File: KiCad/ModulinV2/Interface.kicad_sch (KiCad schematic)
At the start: 51 parts, among them IC2 TL072HIDR, IC3 ADS7041IDCUR, IC4 ADS7866IDBVT, IC42 ADS7041IDCUR, IC5 ADS7866IDBVT, IC6 DAC60501ZDGSR, IC7 DAC60501ZDGSR, IC8 TL074HIDR

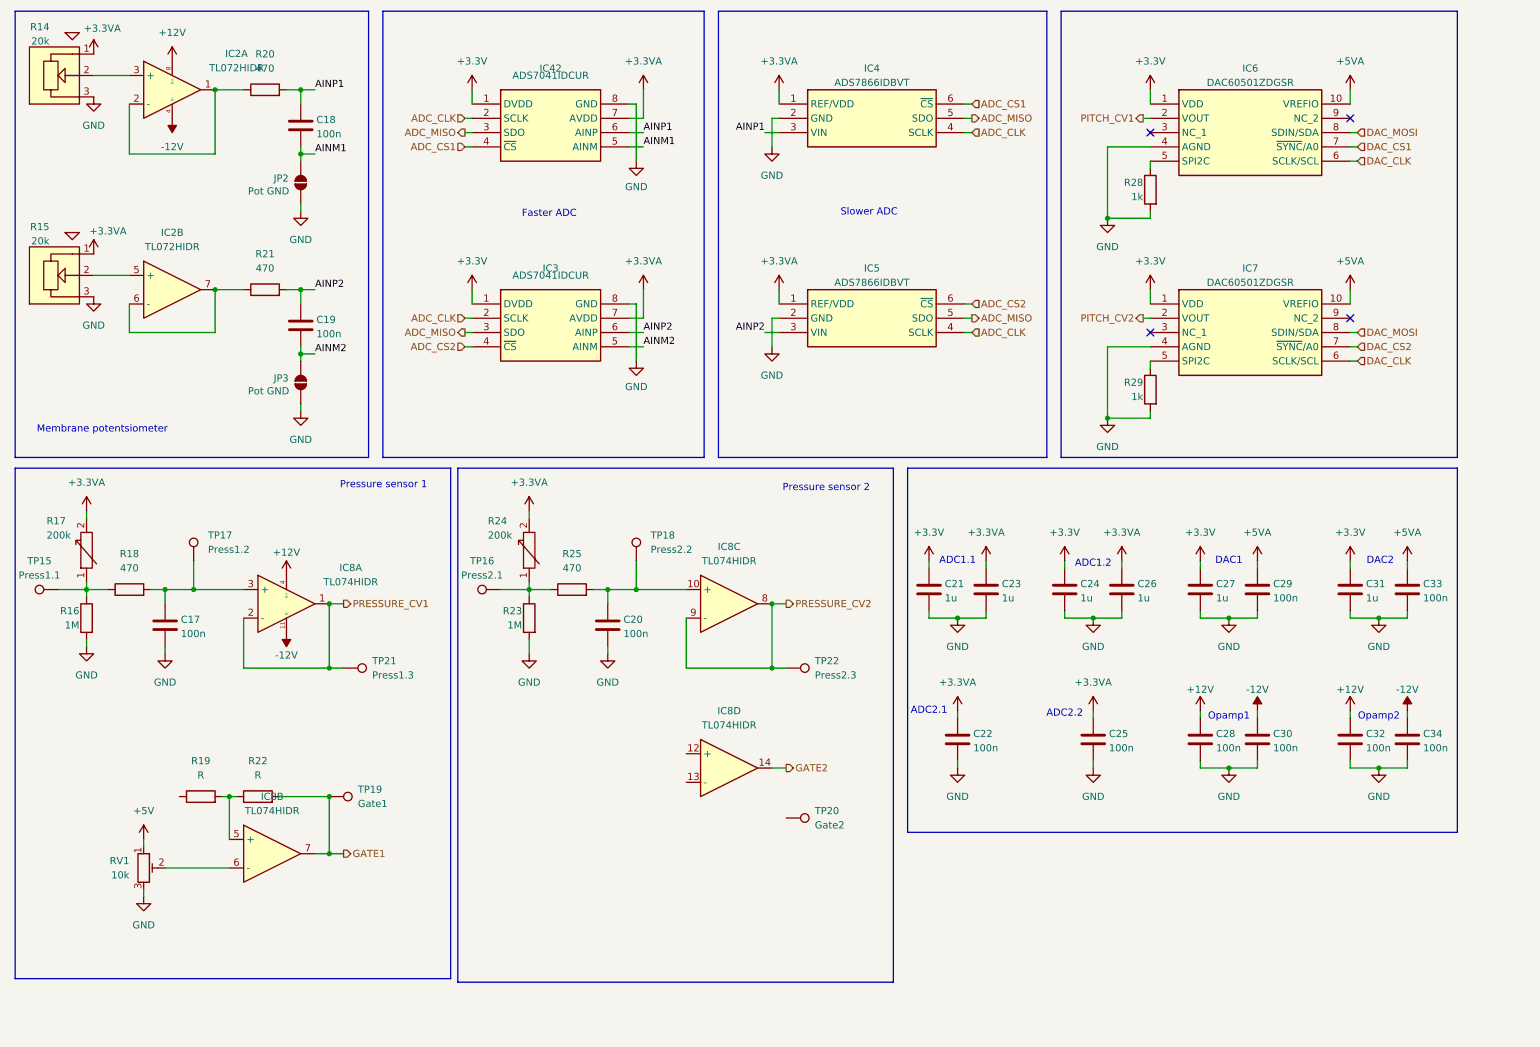
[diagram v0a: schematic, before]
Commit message: Changed switch for the boot and nrst. Fixed the GATE interface trigger
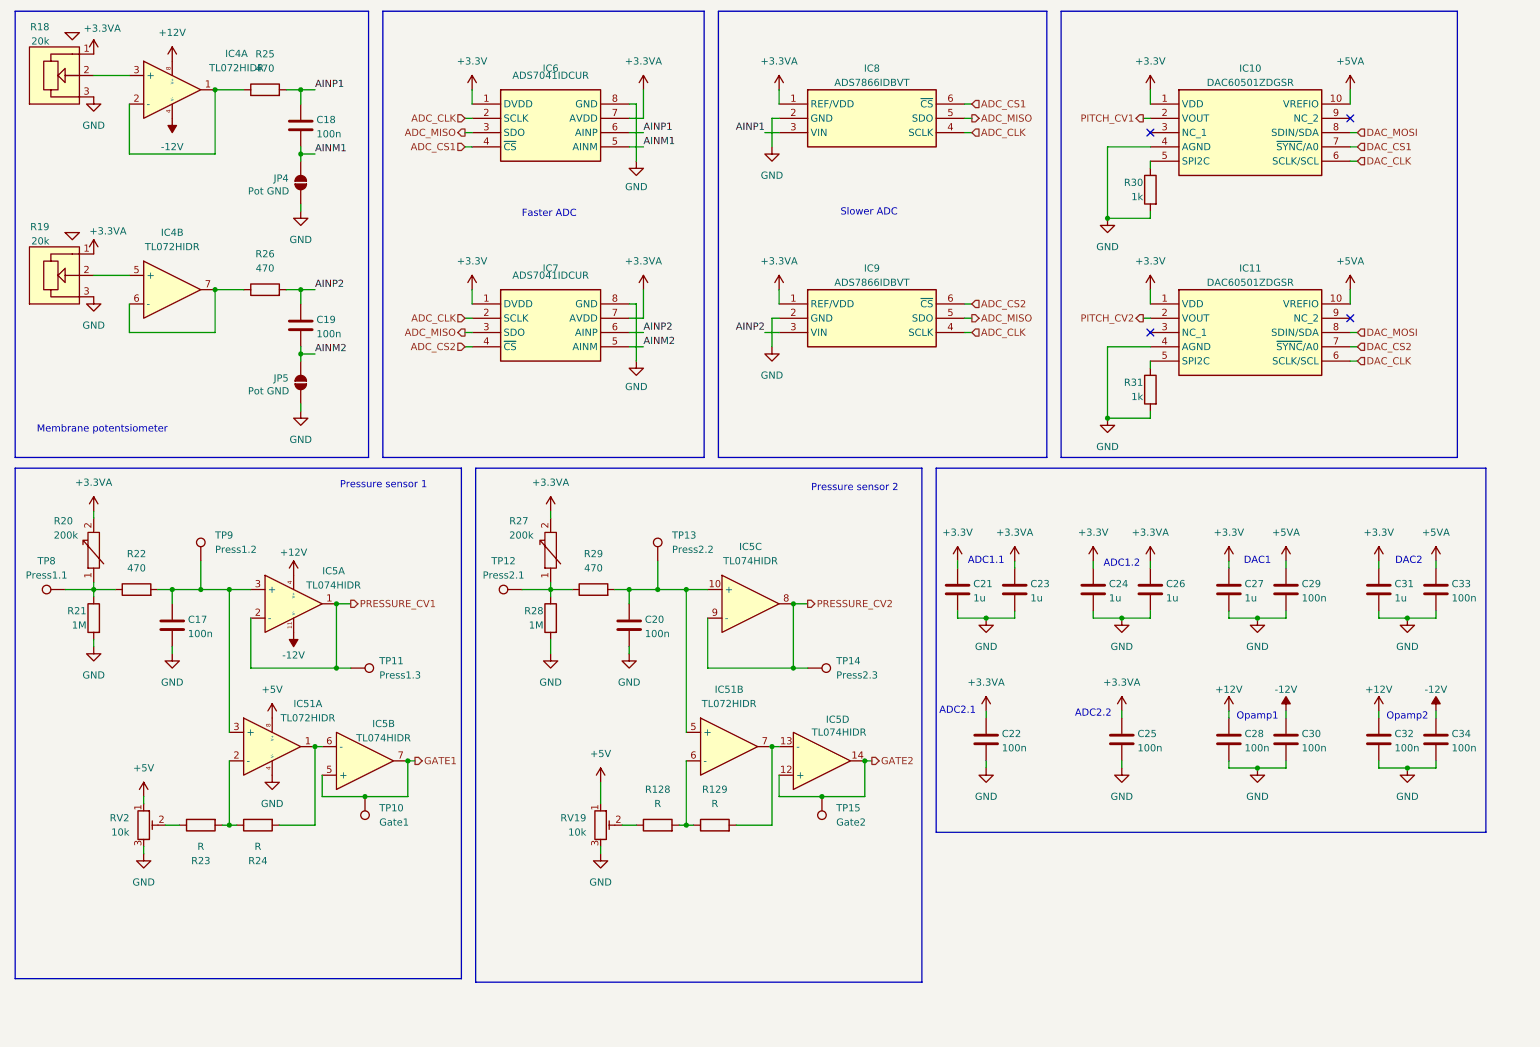
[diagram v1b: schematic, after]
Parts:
- removed IC2: TL072HIDR, SamacSys_Parts:SOIC127P600X175-8N, symbol SamacSys_Parts:TL072HIDR
- added IC4, IC51: TL072HIDR, SOIC127P600X175-8N, symbol SamacSys_Parts:TL072HIDR
- added R128, R129: R, symbol Device:R
- added RV19: 10k, symbol Device:R_Potentiometer_Trim
- renumbered IC6 to IC10, IC7 to IC11, IC8 to IC5, IC42 to IC6, IC3 to IC7, IC4 to IC8, IC5 to IC9, JP2 to JP4, JP3 to JP5, R14 to R18, R15 to R19, R17 to R20, R16 to R21, R18 to R22, R19 to R23, R22 to R24, R20 to R25, R21 to R26, R24 to R27, R23 to R28, R25 to R29, R28 to R30, R29 to R31, RV1 to RV2, TP19 to TP10, TP21 to TP11, TP16 to TP12, TP18 to TP13, TP22 to TP14, TP20 to TP15, TP15 to TP8, TP17 to TP9
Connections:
- net +12V: now also IC4.8 (V+)
- net +5V: now also IC51.8 (V+), RV19.1
- net -12V: now also IC4.4 (V-)
- net GATE1: now also IC5.5 (+); no longer R24.2
- net GATE2: now also IC5.12 (+), TP15.1
- net GND: now also IC51.4 (V-), RV19.3
- net at IC5.13 (-): now also IC51.7, R129.2
- net at C20.1, IC5.10 (+), R29.2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: now also IC51.5 (+)
- net at C17.1, IC5.3 (+), R22.2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: now also IC51.3 (+)
- net at R19.2: now also IC4.5 (+)
- net at R25.1: now also IC4.1, IC4.2 (-)
- net at R18.2: now also IC4.3 (+)
- net at R26.1: now also IC4.6 (-), IC4.7
- net at R23.2, R24.1: now also IC51.2 (-); no longer IC5.5 (+)
- net at IC5.6 (-): now also R24.2, IC51.1; no longer RV2.2
- net at R23.1: now also RV2.2
- new net: IC51.6 (-), R128.2, R129.1
- new net: R128.1, RV19.2
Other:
- moved on the sheet: C17, C20, C21, C22, C23, C24, C25, C26, C27, C28, C29, C30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

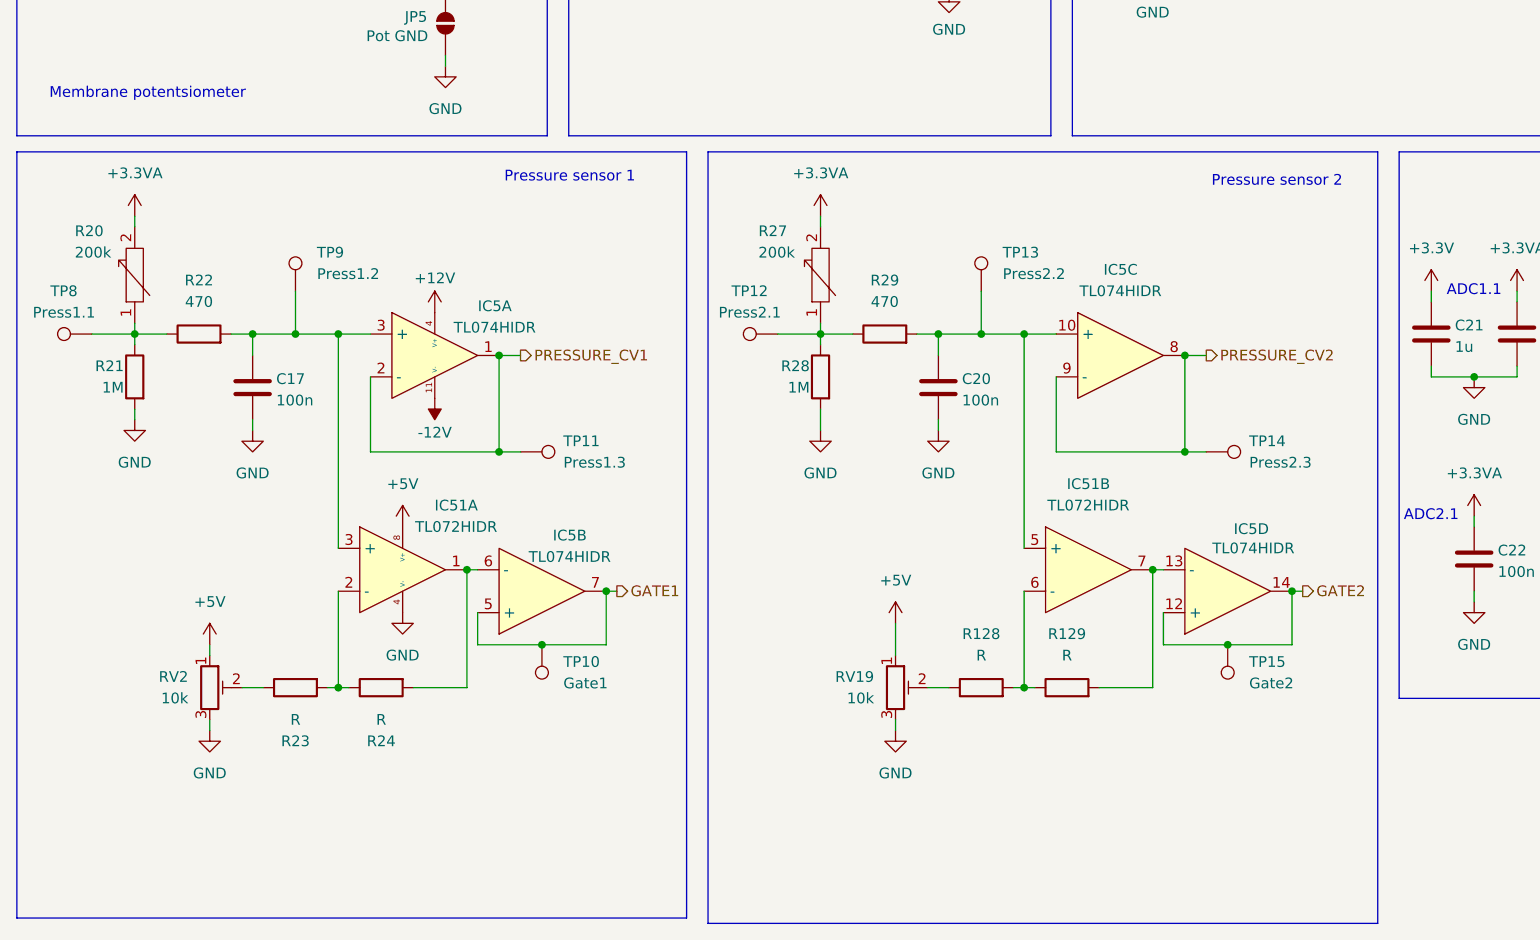
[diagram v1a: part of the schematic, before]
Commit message: Designed the schmitt triger (finally)
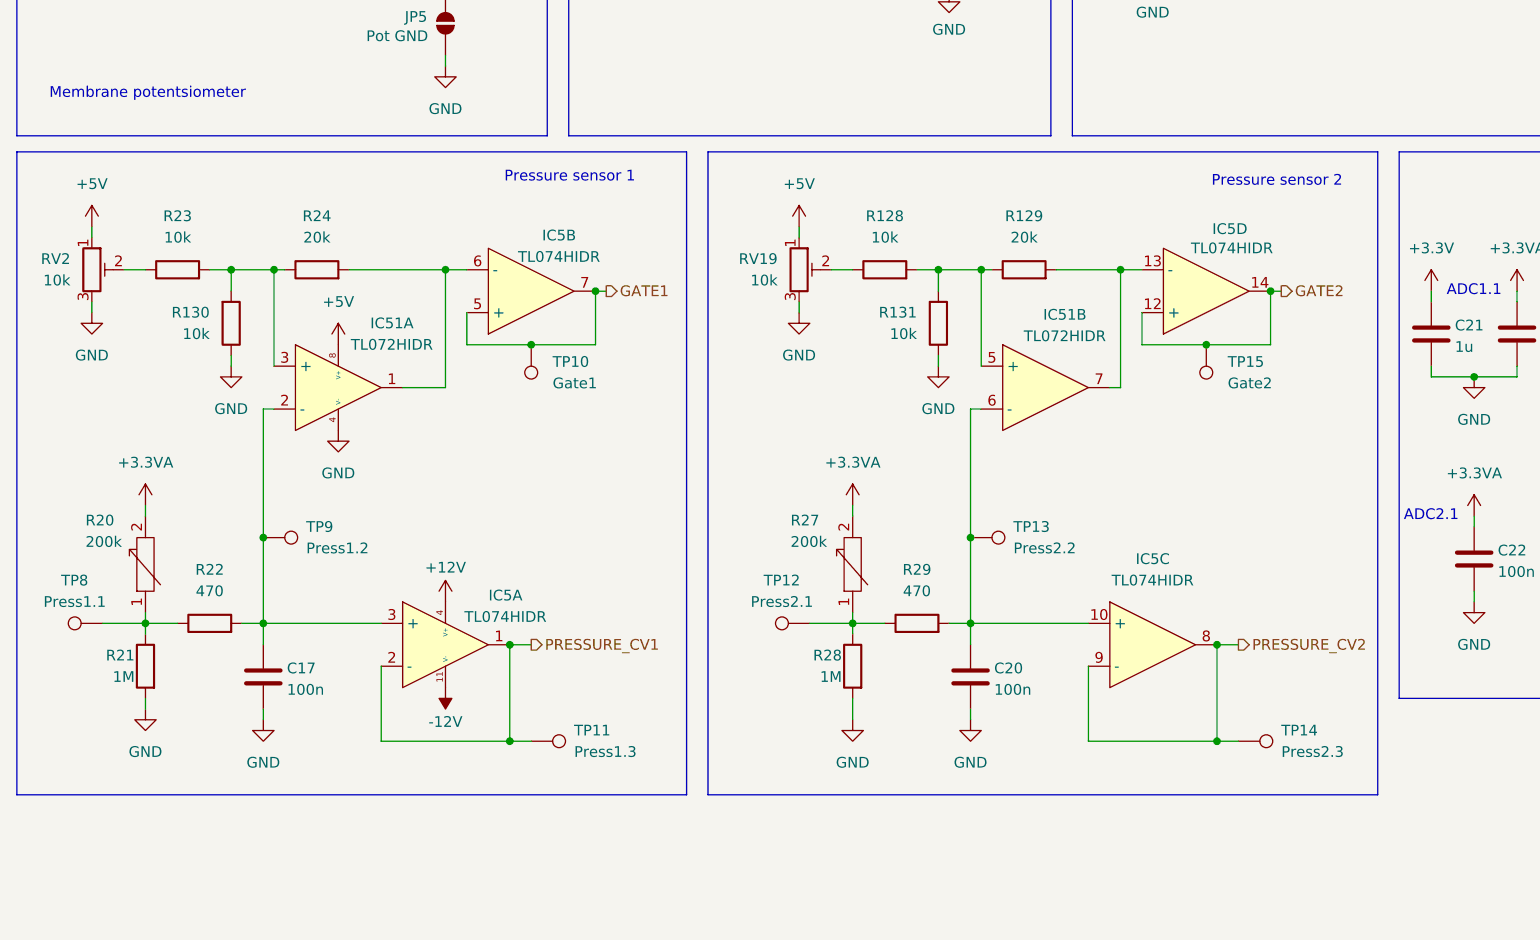
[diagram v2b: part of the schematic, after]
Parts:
- added R130, R131: 10k, symbol Device:R
- IC4, IC51: footprint SOIC127P600X175-8N -> SamacSys_Parts:SOIC127P600X175-8N
- R128, R23: value R -> 10k
- R129, R24: value R -> 20k
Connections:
- net GND: now also R130.1, R131.1
- net at R128.2, R129.1: now also IC51.5 (+), R131.2; no longer IC51.6 (-)
- net at C20.1, IC5.10 (+), R29.2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: now also IC51.6 (-); no longer IC51.5 (+)
- net at C17.1, IC5.3 (+), R22.2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: now also IC51.2 (-); no longer IC51.3 (+)
- net at R23.2, R24.1: now also IC51.3 (+), R130.2; no longer IC51.2 (-)
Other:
- moved on the sheet: C17, C20, IC5A, IC5C, R128, R129, R20, R21, R22, R23, R24, R27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
